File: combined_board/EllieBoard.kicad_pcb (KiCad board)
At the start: 2 copper layers, 222.9 x 165.1 mm, 55 parts

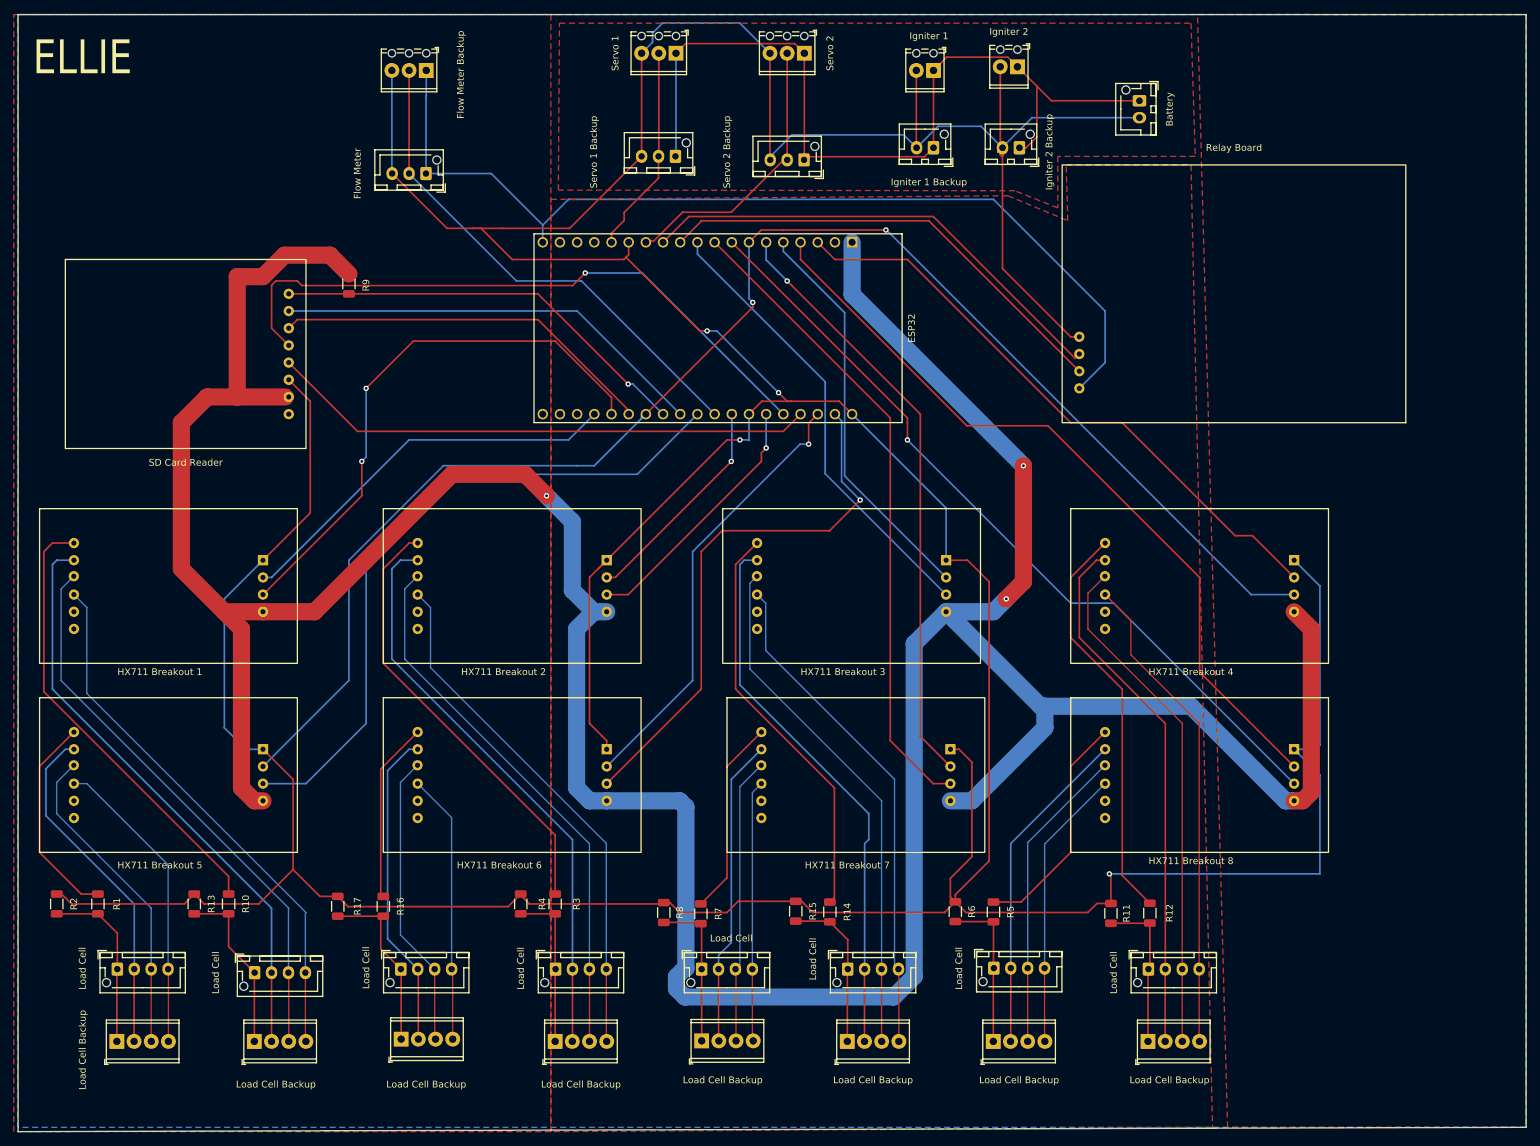
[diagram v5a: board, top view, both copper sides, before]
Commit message: Fixed power pour, added more silkscreen labels, attempted to make board less massive
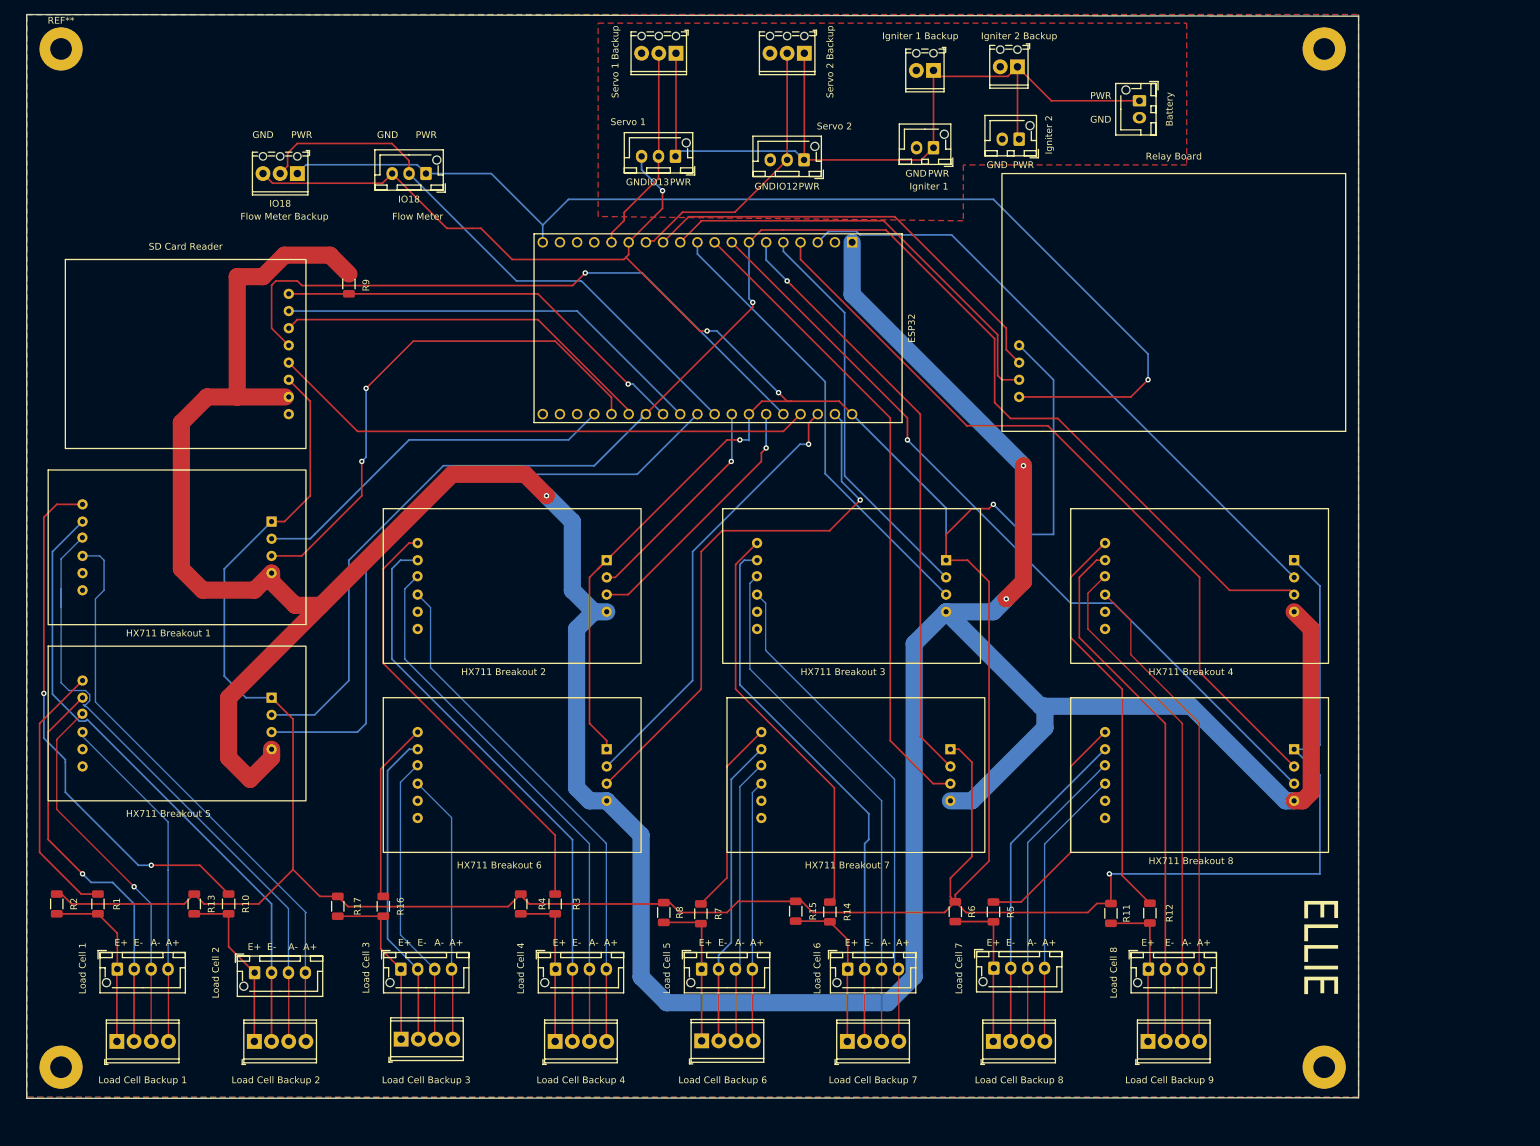
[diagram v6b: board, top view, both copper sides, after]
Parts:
- added ?: , , F.Cu at (212.1, 168.9)
- added ?: , , F.Cu at (212.1, 18.4)
- added ?: , , F.Cu at (25.4, 168.9)
- added REF**: MountingHole_3.2mm_M3_Pad, MountingHole:MountingHole_3.2mm_M3_Pad, F.Cu at (25.4, 18.4)
- Igniter 1 : renamed from Igniter 1 Backup
- Igniter 1 Backup: renamed from Igniter 1
- Igniter 2 : renamed from Igniter 2 Backup
- Igniter 2 Backup: renamed from Igniter 2
- Load Cell 1: renamed from Load Cell 
- Load Cell 2: renamed from Load Cell 
- Load Cell 3: renamed from Load Cell 
- Load Cell 4: renamed from Load Cell
- Load Cell 5: renamed from Load Cell 
- Load Cell 6: renamed from Load Cell 
- Load Cell 7: renamed from Load Cell 
- Load Cell 8: renamed from Load Cell 
- Load Cell Backup 1: renamed from Load Cell Backup
- Load Cell Backup 2: renamed from Load Cell Backup
- Load Cell Backup 3: renamed from Load Cell Backup
- Load Cell Backup 4: renamed from Load Cell Backup
- Load Cell Backup 6: renamed from Load Cell Backup
- Load Cell Backup 7: renamed from Load Cell Backup
- Load Cell Backup 8: renamed from Load Cell Backup
- Load Cell Backup 9: renamed from Load Cell Backup
- Servo 1 : renamed from Servo 1 Backup
- Servo 1 Backup: renamed from Servo 1
- Servo 2 : renamed from Servo 2 Backup
- Servo 2 Backup: renamed from Servo 2 
- moved Flow Meter Backup 24.4 mm to (60.3, 36.8)
- moved Relay Board 8.98 mm to (189.9, 57.1)
- moved HX711 Breakout 5 7.73 mm to (41.3, 119.4)
- moved HX711 Breakout 1 5.85 mm to (41.3, 93.3)
- moved Igniter 2  1.27 mm to (167.0, 31.8)
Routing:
- net GND: track 828.9 -> 698.7 mm, vias 4 -> 6
- net +5V: track 142.7 -> 167.5 mm, vias 0 -> 1
- net Net-(R10-Pad2): track 66.9 -> 78.8 mm, vias 0 -> 2
- net A2-: track 83.5 -> 95.0 mm
- net IO18: track 74.7 -> 84.4 mm
- net u1: track 51.0 -> 60.0 mm, vias 0 -> 1
- net Net-(R1-Pad2): track 31.1 -> 39.2 mm
- net A1-: track 47.7 -> 55.8 mm, vias 0 -> 1
- net A2+: track 80.3 -> 88.0 mm
- net IO14: track 72.0 -> 65.0 mm
- net A1+: track 45.1 -> 51.0 mm
- net u2: track 87.3 -> 93.1 mm
- net IO27: track 69.5 -> 64.7 mm
- net +3V3: track 548.6 -> 553.3 mm
- net IO5: track 100.2 -> 95.8 mm
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- added copper zone on B.Cu, net (none)
- removed copper zone on B.Cu, net GND
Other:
- board size 222.9 x 165.1 mm -> 196.8 x 160.2 mm
- board text added: "A+"
- board text added: "A-"
- board text added: "E+"
- board text added: "E-"
- board text added: "GND"
- board text added: "IO12"
- board text added: "IO13"
- board text added: "IO18"
- board text added: "PWR"

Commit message: last few edits to layout
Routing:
- net +5V: track 167.5 -> 169.2 mm

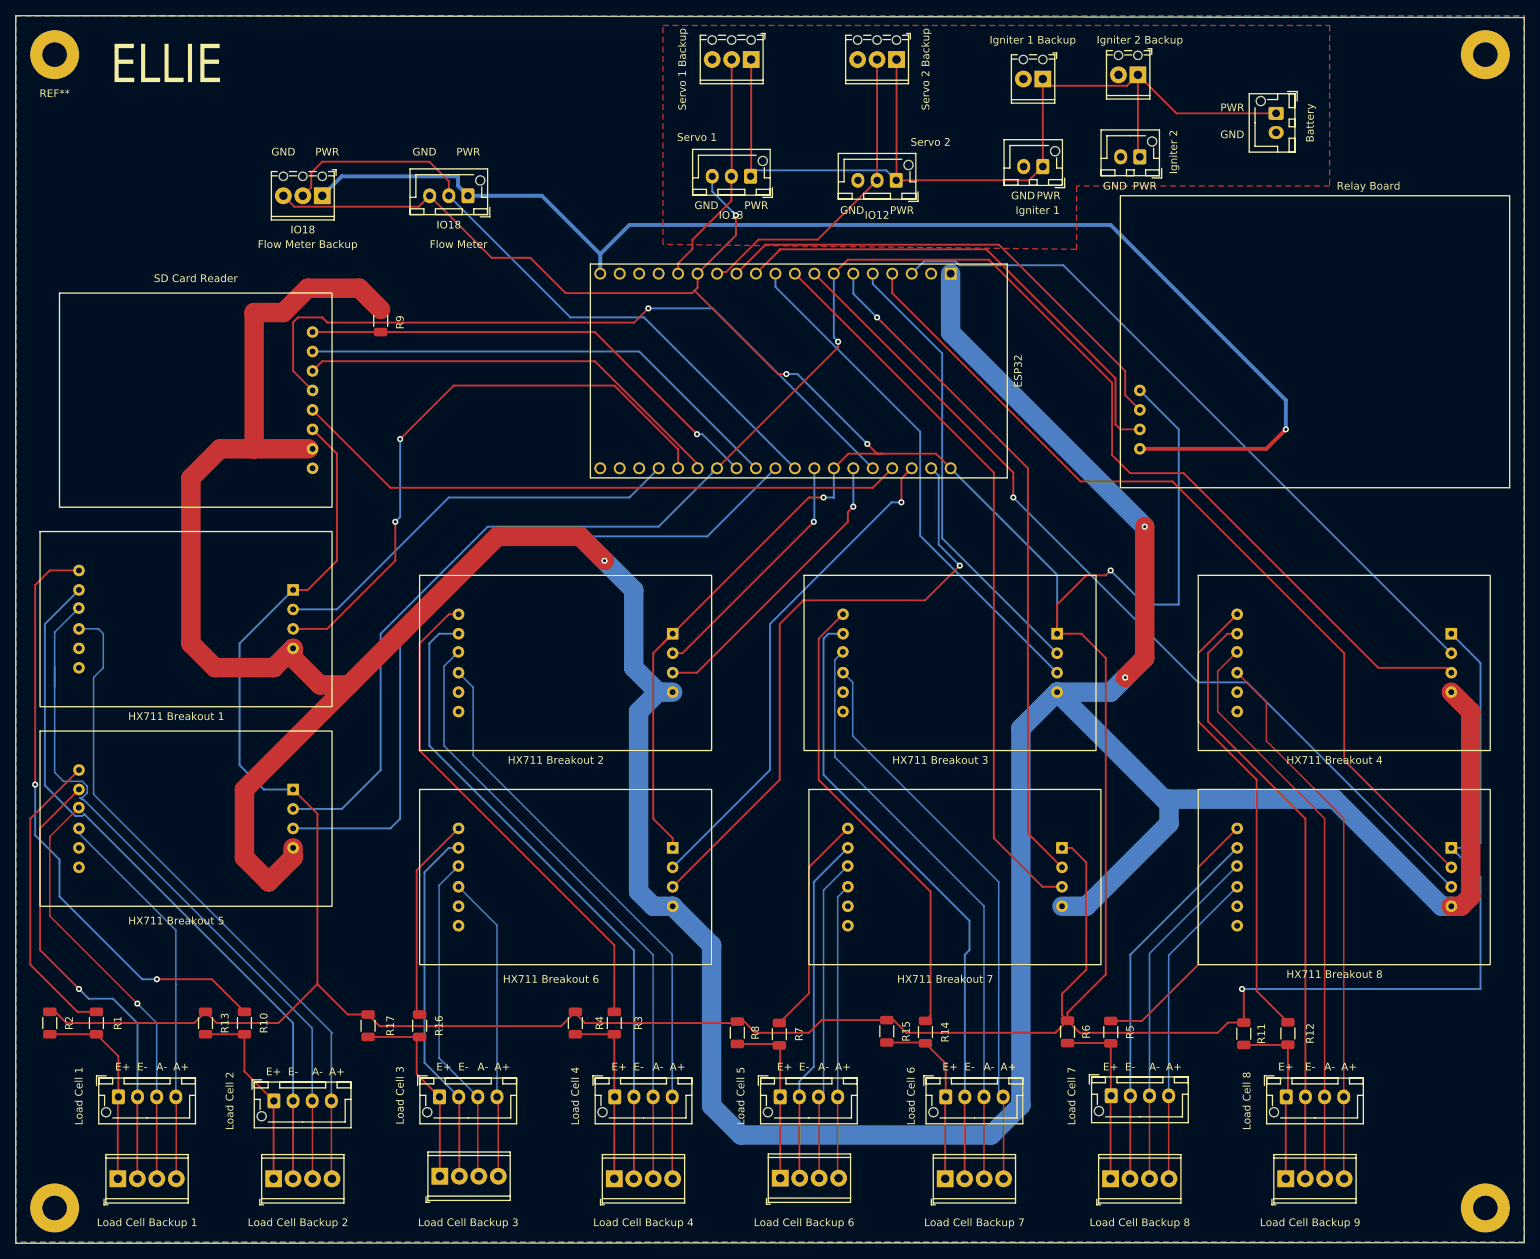
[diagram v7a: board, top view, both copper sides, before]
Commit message: adding vias fixing solder mask
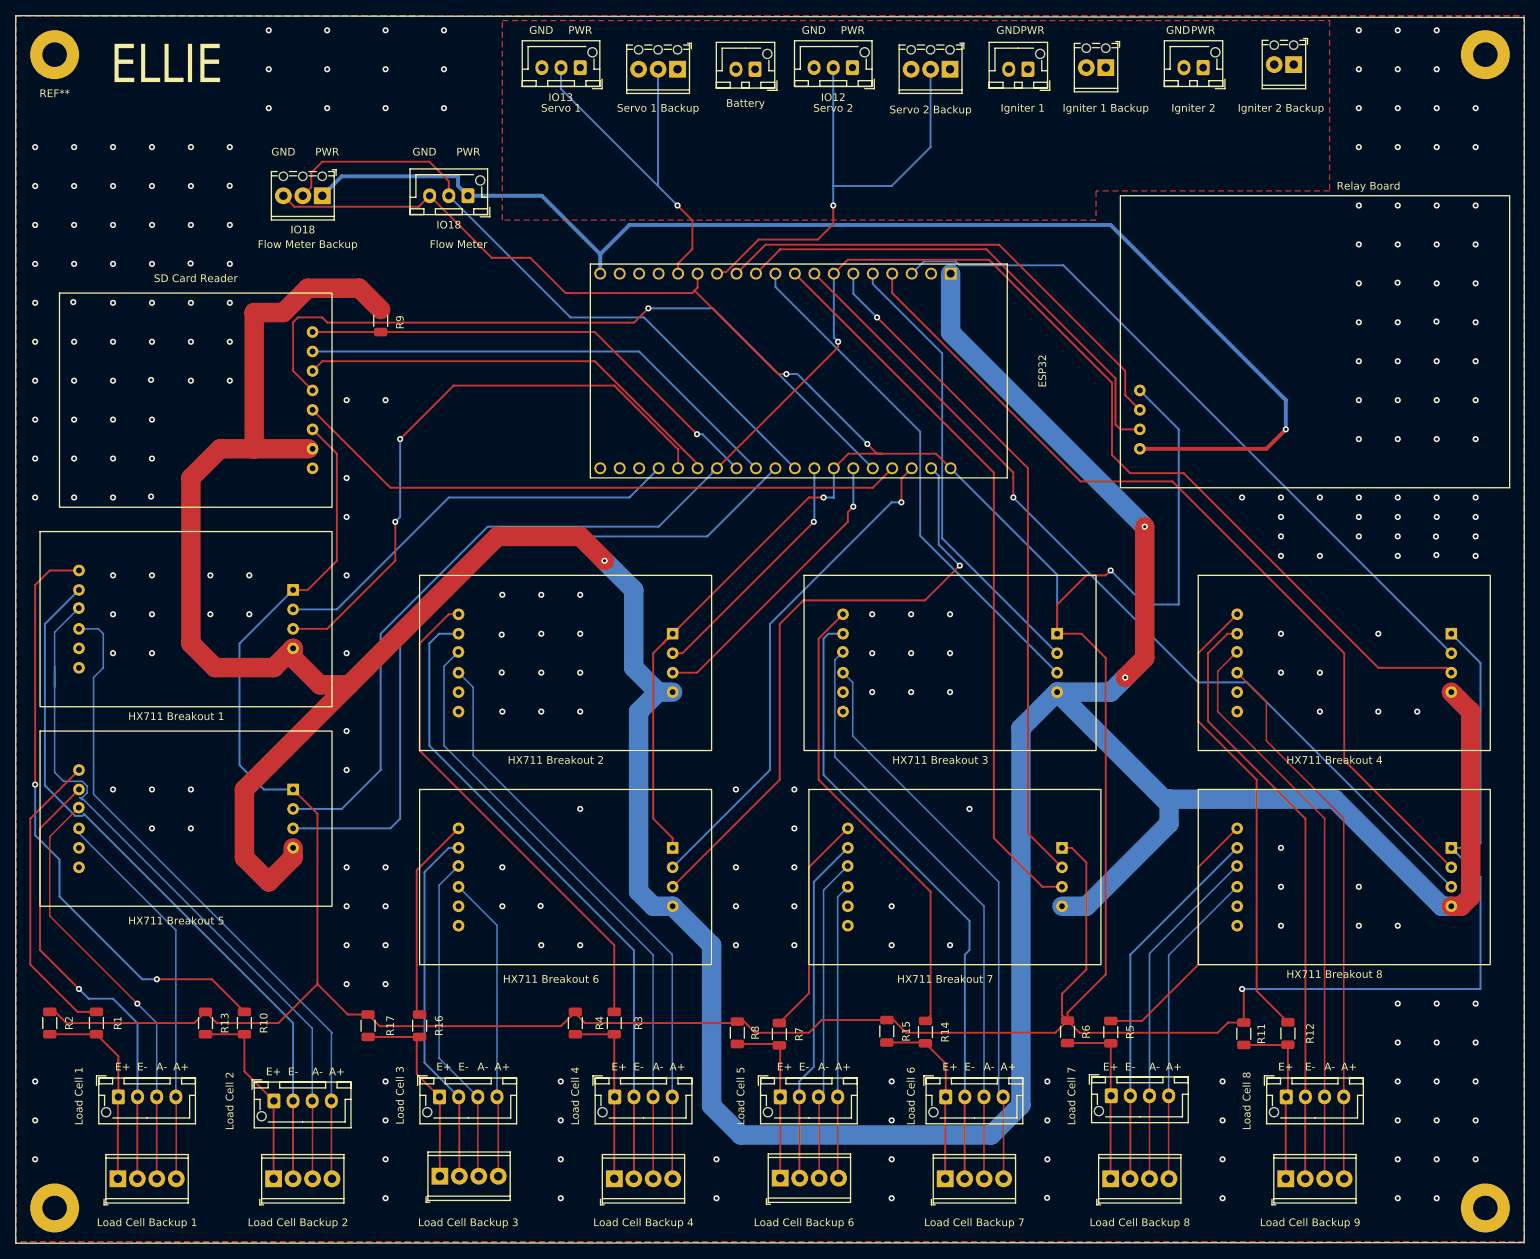
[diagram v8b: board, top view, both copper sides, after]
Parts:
- moved Battery 68.2 mm to (116.8, 20.3), turned to 180 degrees
- moved Servo 1  26.4 mm to (94.0, 20.1)
- moved Igniter 2 Backup 20.4 mm to (187.1, 19.7)
- moved Servo 2  15.8 mm to (129.5, 20.1)
- moved Igniter 2  14.3 mm to (175.3, 20.1)
- moved Igniter 1  12.8 mm to (152.4, 20.3)
- moved Servo 1 Backup 9.69 mm to (106.7, 20.3)
- moved Igniter 1 Backup 8.35 mm to (162.6, 20.1)
- moved Servo 2 Backup 7.10 mm to (142.2, 20.3)
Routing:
- net Lipo: track 126.5 -> 0.00 mm
- net IO12: track 41.5 -> 63.0 mm, vias 0 -> 1
- net IO13: track 30.8 -> 50.0 mm, vias 0 -> 1
- net GND: track 698.7 -> 682.6 mm, vias 6 -> 261
- added copper zone on B.Cu, net GND
- removed copper zone on B.Cu, net (none)
